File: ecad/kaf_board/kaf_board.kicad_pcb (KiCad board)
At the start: 4 copper layers, 116 x 71 mm, 234 parts, among them J1 PWR, J2 TEC1, J3 Conn_01x12, J4 TEC2, J5 USB, J6 TECPWR, M1 Motor_Servo, M2 Servo cut-out, Q1 MMBT3904LT1G, Q2 NTD4804N, Q3 NTD4804N, U1 MAX4649, U10 LM224, U11 LM224, U12 LM224, U13 LD1117S12CTR_SOT223, U14 LD1117S33CTR_SOT223, U15 LTC3265*FE, U16 93LCxxBxxOT, U17 FT2232HL, U18 ICE40HX1K-VQ100, U19 W25X20CL, U2 ADP7118AUJZ, U20 MCP3004, U21 TC4427, U3 AD9826, U4 KAF-CDIP24, U5 TL432LIAIDBZR, U6 TL432LIAIDBZR, U7 TC4427, U8 TC4427, U9 TC4428, X1 KC7050A-C3, Y1 12 MHz

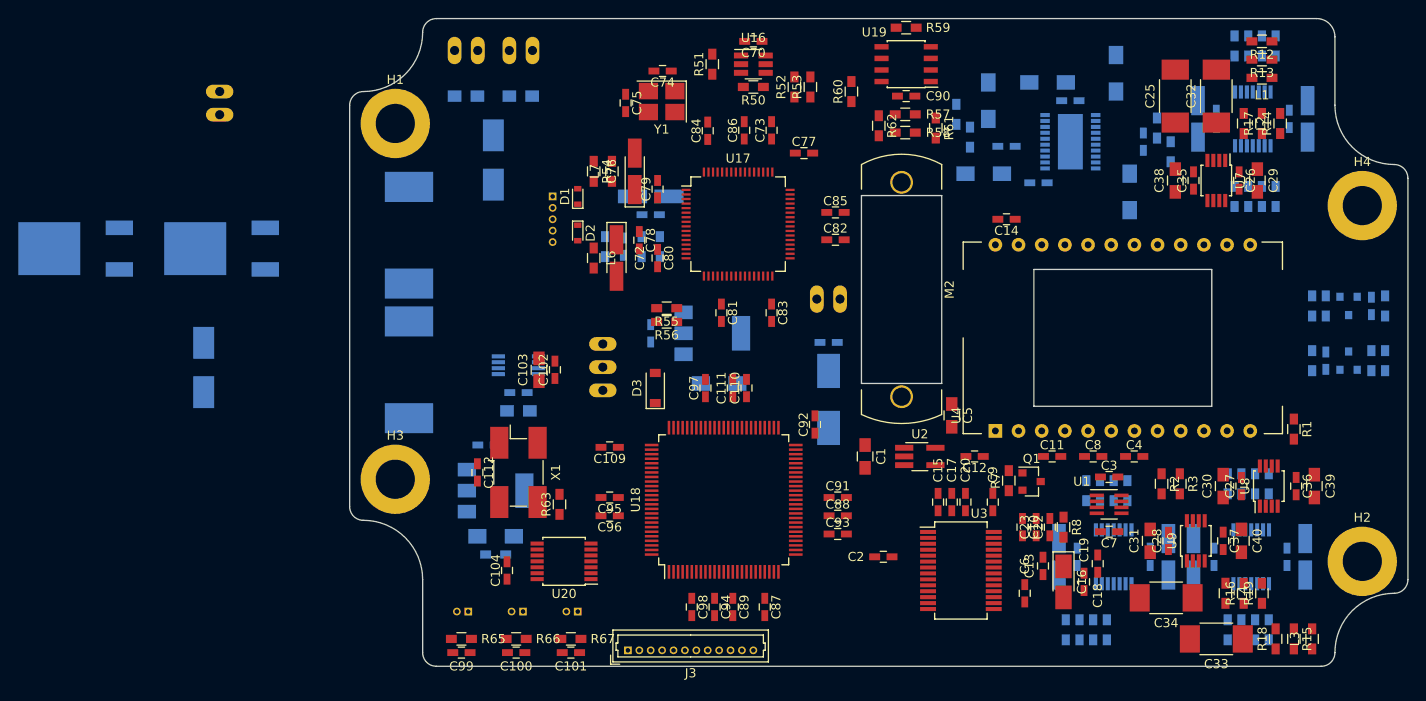
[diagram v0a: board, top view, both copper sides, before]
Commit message: Started routing PCB
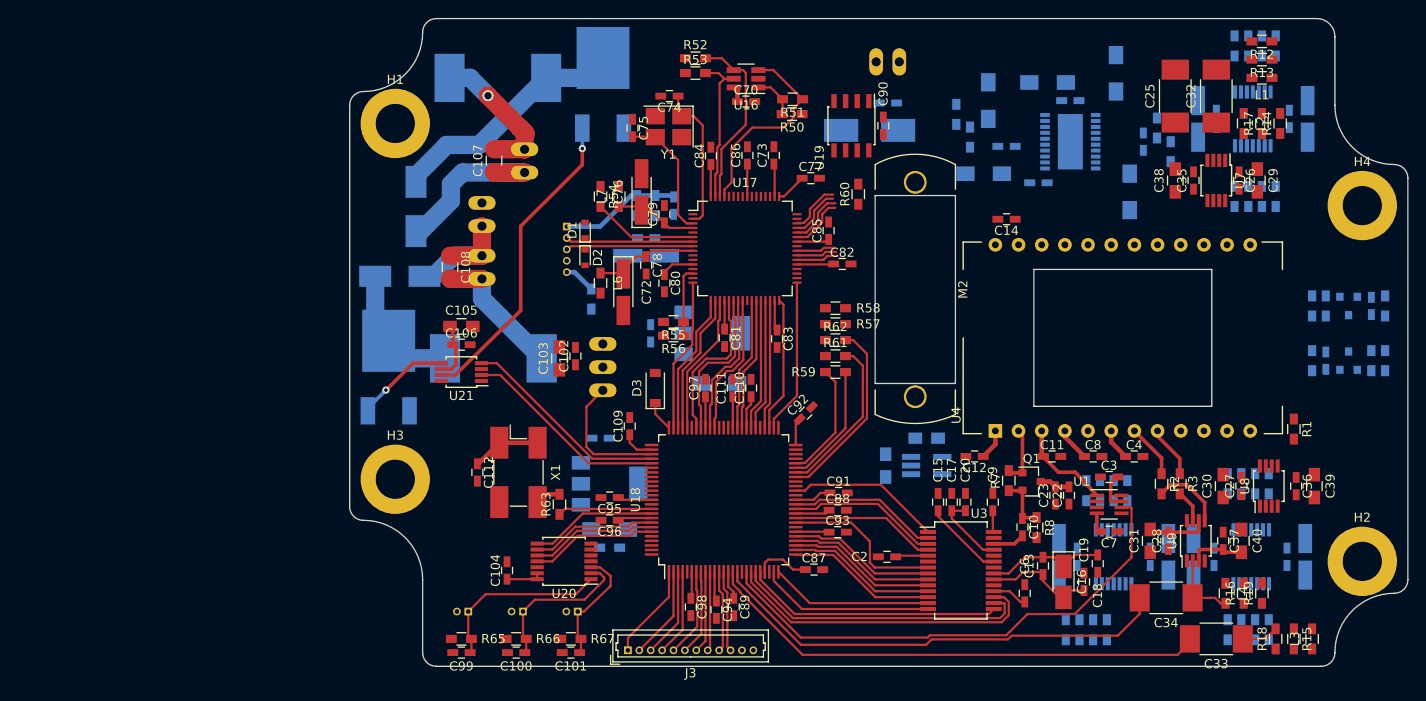
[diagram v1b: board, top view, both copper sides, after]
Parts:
- C1, C5, U2: moved to B.Cu
- C105, C106, C107, C108, U21: moved to F.Cu
- moved Q2 53.1 mm to (117.5, 79.0), turned to 270 degrees
- moved R59 38.5 mm to (145.2, 105.8), turned to 0 degrees
- moved J6 32.3 mm to (106.5, 89.8), turned to 90 degrees
- moved C69 29.8 mm to (149.0, 79.2), turned to 180 degrees
- moved R61 27.3 mm to (145.2, 104.0), turned to 0 degrees
- moved C68 27.0 mm to (151.0, 76.2)
- moved J1 26.8 mm to (152.2, 71.8)
- moved R57 24.2 mm to (145.2, 100.5)
- moved R62 24.0 mm to (145.2, 102.2), turned to 0 degrees
- moved D5 23.7 mm to (97.5, 95.2), turned to 180 degrees
- moved J4 22.7 mm to (106.5, 93.0), turned to 270 degrees
- moved R58 20.7 mm to (145.2, 98.8)
- moved C108 20.3 mm to (103.0, 94.2), turned to 270 degrees
- moved L8 19.8 mm to (108.2, 73.5), turned to 90 degrees
- moved Q3 19.2 mm to (94.0, 110.0), turned to 270 degrees
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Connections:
- Q2 pad 2: (no net) -> Net-(D4-Pad2)
- Q3 pad 2: (no net) -> Net-(D5-Pad2)
- R55 pad 2: (no net) -> /usb-interface/VUSB
- U18 pad 100: /fpga/PWM_SERVO -> (no net)
- U18 pad 15: /ccd/AMP_OFF -> /ccd/R_3.3V
- U18 pad 18: /ccd/R_3.3V -> /ccd/AMP_OFF
- U18 pad 78: (no net) -> /fpga/PWM_SERVO
- U18 pad 79: (no net) -> /fpga/PWM_TEC2
- U18 pad 80: (no net) -> /fpga/PWM_TEC1
- U18 pad 97: /fpga/PWM_TEC1 -> (no net)
- U18 pad 99: /fpga/PWM_TEC2 -> (no net)
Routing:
- net +3V3: track 0.00 -> 71.7 mm
- net /ccd/AMP_OFF: track 0.00 -> 56.1 mm
- net /ccd/R_3.3V: track 0.00 -> 55.7 mm
- net /ccd/H_3.3V: track 0.00 -> 51.2 mm
- net /thermo_and_mechanical/V_TEC: track 0.00 -> 39.2 mm
- net /ccd/AD_SLOAD: track 0.00 -> 34.8 mm
- net Net-(Q2-Pad1): track 0.00 -> 34.4 mm, vias 0 -> 1
- net /ccd/AD_SCLK: track 0.00 -> 32.5 mm
- net Net-(D4-Pad2): track 0.00 -> 28.5 mm
- net /ccd/AD_SDATA: track 0.00 -> 28.2 mm
- net /usb-interface/FT_CDONE: track 0.00 -> 26.3 mm
- net /usb-interface/FT_CRESET: track 0.00 -> 23.6 mm
- net /fpga/PWM_TEC2: track 0.00 -> 23.0 mm
- net /fpga/PWM_TEC1: track 0.00 -> 22.7 mm
- net Net-(R51-Pad1): track 0.00 -> 22.4 mm
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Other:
- outline, holes or cut-outs redrawn

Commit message: continued routing
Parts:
- moved R60 24.4 mm to (146.6, 110.6)
- moved C90 22.1 mm to (142.6, 99.4), turned to 270 degrees
- moved U19 20.6 mm to (146.1, 99.3), turned to 90 degrees
- moved R61 12.0 mm to (151.8, 114.0), turned to 180 degrees
- moved R62 11.2 mm to (150.3, 112.3), turned to 180 degrees
- moved R59 9.09 mm to (146.1, 114.8)
- moved R58 8.19 mm to (143.5, 106.8)
- moved R57 7.90 mm to (143.5, 108.2)
- moved R19 4.00 mm to (188.0, 130.0), turned to 270 degrees
- moved L3 2.25 mm to (195.2, 135.0)
- moved L4 1.75 mm to (189.8, 130.0)
- moved C82 1.53 mm to (144.5, 94.2)
- moved R15 1.50 mm to (197.0, 135.0)
- moved R16 1.50 mm to (191.5, 130.0)
- moved C85 1.35 mm to (145.0, 91.5), turned to 0 degrees
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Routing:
- net /fpga/V1_3.3V: track 0.00 -> 77.0 mm
- net /ccd/V1_3.3V: track 0.00 -> 74.9 mm
- net /usb-interface/FT_SCK: track 4.65 -> 36.2 mm
- net Net-(R1-Pad1): track 0.00 -> 24.0 mm
- net /usb-interface/FT_SS: track 6.07 -> 27.8 mm, vias 0 -> 2
- net /usb-interface/FT_CRESET: track 23.6 -> 42.8 mm
- net /usb-interface/FT_MOSI: track 17.9 -> 36.2 mm
- net Net-(C33-Pad1): track 4.06 -> 19.8 mm
- net /usb-interface/FT_CDONE: track 26.3 -> 41.8 mm, vias 0 -> 2
- net /usb-interface/FT_MISO: track 17.1 -> 30.6 mm, vias 0 -> 2
- net Net-(R60-Pad2): track 0.00 -> 13.5 mm
- net /ccd/V_RH: track 0.00 -> 6.79 mm
- net Net-(R57-Pad1): track 0.00 -> 6.37 mm
- net (no net): track 6.07 -> 0.00 mm
- net Net-(C25-Pad1): track 0.00 -> 5.61 mm
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
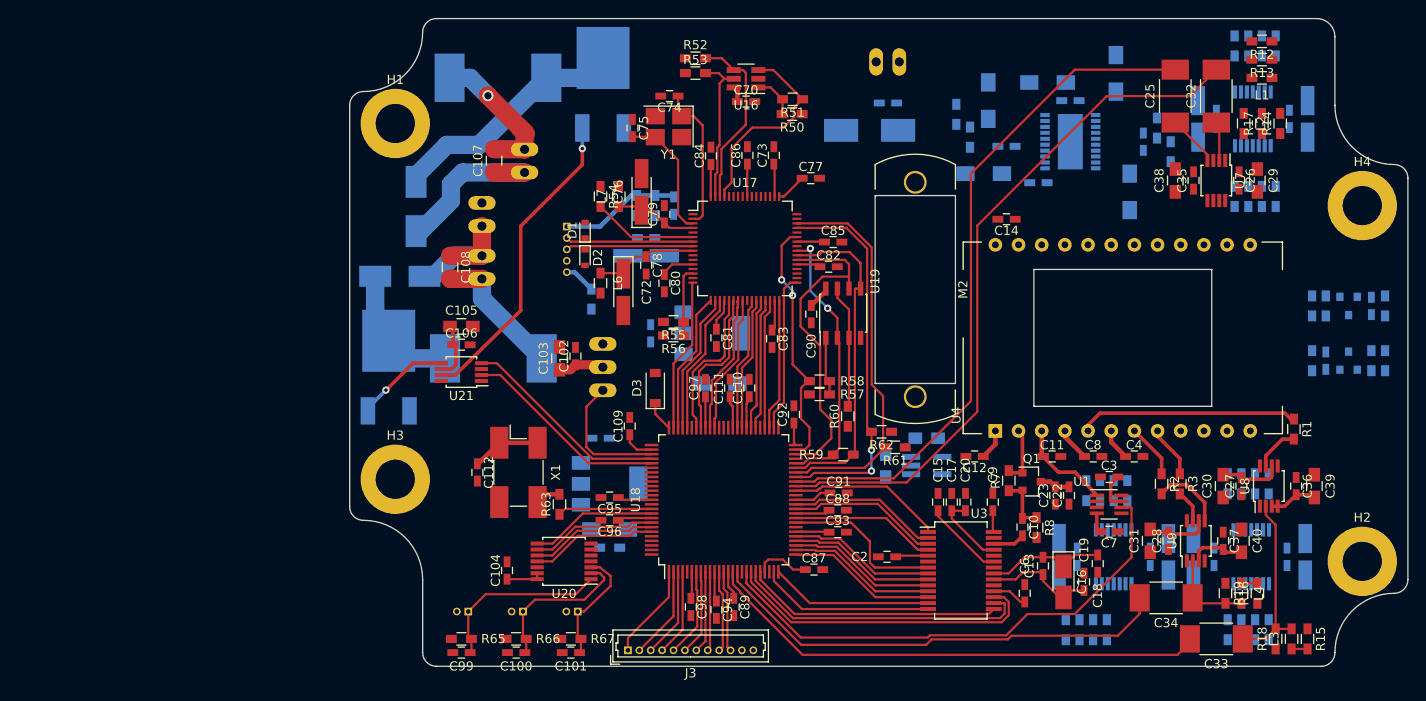
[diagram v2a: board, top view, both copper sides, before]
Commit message: Changed +-15 DC/DC converter and routed it.
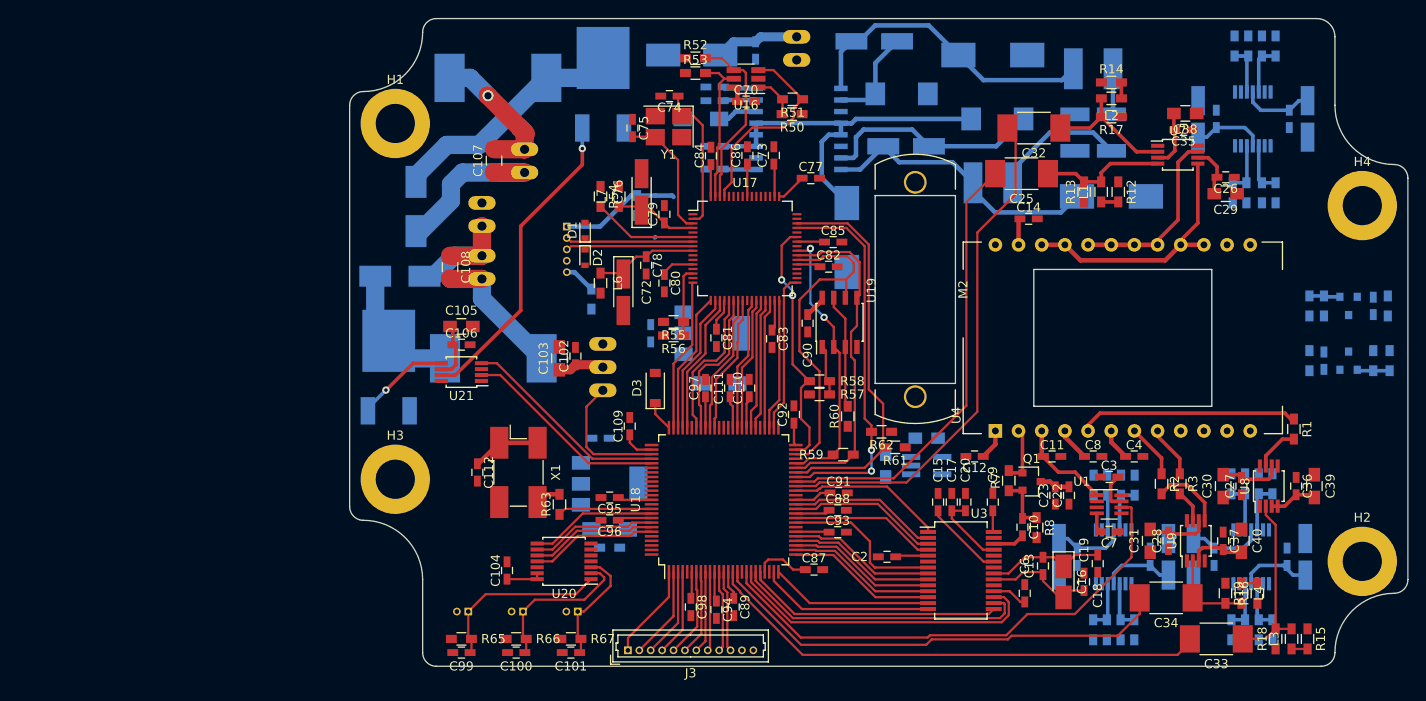
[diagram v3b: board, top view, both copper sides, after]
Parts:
- removed C67: 4.7u, Capacitors_Tantalum_SMD:CP_Tantalum_Case-A_EIA-3216-18_Hand
- removed C71: 10n, Capacitors_SMD:C_0603_HandSoldering
- removed R45, R48: 604k, Resistors_SMD:R_0603_HandSoldering
- removed R46, R47: 52.3k, Resistors_SMD:R_0603_HandSoldering
- added D6: SS14, Diodes_SMD:D_SMA_Handsoldering, B.Cu at (153.0, 81.0)
- added D7: SS14, Diodes_SMD:D_SMA_Handsoldering, B.Cu at (149.5, 69.5)
- added L10: 100u, kaf_board:L_Bourns_SRR0604, B.Cu at (152.5, 75.2)
- added L11: 33u, kaf_board:L_Wuerth_LQS_5040, B.Cu at (162.5, 85.0)
- added L12: 33u, kaf_board:L_Wuerth_LQS_5040, B.Cu at (173.5, 72.5)
- C53: value 10u -> 10n; footprint Capacitors_SMD:C_1206_HandSoldering -> Capacitors_SMD:C_0603_HandSoldering
- C54: value 10u -> 0.1u; footprint Capacitors_SMD:C_1206_HandSoldering -> Capacitors_SMD:C_0603_HandSoldering
- C55: value 1u -> 10u; footprint Capacitors_SMD:C_0603_HandSoldering -> Capacitors_SMD:C_1206_HandSoldering
- C56: value 10u -> 1u; footprint Capacitors_SMD:C_1206_HandSoldering -> Capacitors_SMD:C_0603_HandSoldering
- C59: value 1u -> 10n
- C62, C63: value 10u -> 100u; footprint Capacitors_SMD:C_1206_HandSoldering -> Capacitors_Tantalum_SMD:CP_Tantalum_Case-D_EIA-7343-31_Hand
- C64: value 0.1u -> 100u; footprint Capacitors_SMD:C_0603_HandSoldering -> Capacitors_Tantalum_SMD:CP_Tantalum_Case-D_EIA-7343-31_Hand
- C65, C66: value 0.1u -> 2.2u; footprint Capacitors_SMD:C_0603_HandSoldering -> Capacitors_Tantalum_SMD:CP_Tantalum_Case-A_EIA-3216-18_Hand
- L5: value 1K/0.8A -> 100u; footprint Inductors_SMD:L_0603_HandSoldering -> kaf_board:L_Bourns_SRR0604
- U15: value LTC3265*FE -> MAX743; footprint kaf_board:TSSOP-20-1EP_4.4x6.5mm_P0.65mm -> Housings_SOIC:SOIC-16W_7.5x10.3mm_Pitch1.27mm
- moved C66 50.8 mm to (173.5, 77.5), turned to 0 degrees
- moved C54 44.7 mm to (132.0, 81.0), turned to 180 degrees
- moved C55 40.5 mm to (130.5, 78.0)
- moved L5 38.7 mm to (163.0, 78.0)
- moved C59 37.0 mm to (132.0, 74.5), turned to 180 degrees
- moved C56 36.6 mm to (132.0, 76.0), turned to 180 degrees
- moved U15 29.8 mm to (141.2, 79.1), turned to 0 degrees
- moved C53 29.5 mm to (132.0, 83.5)
- moved R13 24.3 mm to (172.5, 86.0), turned to 90 degrees
- moved R12 22.8 mm to (176.2, 86.0), turned to 270 degrees
- moved L1 21.6 mm to (174.4, 86.0), turned to 90 degrees
- moved C62 21.6 mm to (146.5, 91.0), turned to 270 degrees
- moved C63 21.2 mm to (162.5, 71.0), turned to 180 degrees
- moved C69 21.2 mm to (129.5, 71.0)
- moved C32 20.3 mm to (167.0, 79.0), turned to 180 degrees
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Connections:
- net Net-(C76-Pad1) renamed /usb-interface/VPHY
- net Net-(D3-Pad1) renamed /fpga/VPP_2V5
- C1 pad 2: +12V -> +6V
- C102 pad 1: +5V -> +6V
- C103 pad 1: +5V -> +6V
- C53 pad 1: +12V -> Net-(C53-Pad1)
- C54 pad 1: Net-(C54-Pad1) -> +6V
- C55 pad 2: Net-(C55-Pad2) -> GND
- C57 pad 1: +5V -> +6V
- C58 pad 1: +5V -> +6V
- C59 pad 2: Net-(C59-Pad2) -> GND
- C62 pad 1: -15V -> +6V
- C63 pad 1: +15V -> GND
- C63 pad 2: GND -> Net-(C63-Pad2)
- C65 pad 1: GND -> +15V
- C65 pad 2: Net-(C65-Pad2) -> GND
- C66 pad 1: +5V -> GND
- C66 pad 2: GND -> -15V
- C68 pad 1: +12V -> +6V
- C69 pad 1: +12V -> +6V
- J1 pad 1: +12V -> +6V
- L5 pad 1: /usb-interface/VUSB -> +6V
- L5 pad 2: +5V -> Net-(D6-Pad2)
- M1 pad 2: +5V -> +6V
- U13 pad 3: +5V -> +6V
- U14 pad 3: +5V -> +6V
- U15 pad 1: Net-(C59-Pad2) -> Net-(C53-Pad1)
- U15 pad 10: Net-(C55-Pad2) -> Net-(D7-Pad1)
- U15 pad 11: Net-(C55-Pad1) -> GND
- U15 pad 12: Net-(C55-Pad1) -> +6V
- U15 pad 13: Net-(C54-Pad1) -> +6V
- U15 pad 15: +12V -> Net-(D6-Pad2)
- U15 pad 16: GND -> Net-(C64-Pad1)
- U15 pad 2: Net-(C59-Pad2) -> GND
- U15 pad 3: Net-(C59-Pad1) -> +6V
- U15 pad 4: +12V -> +6V
- U15 pad 5: +12V -> +6V
- U15 pad 6: Net-(C65-Pad2) -> Net-(C55-Pad1)
- U15 pad 7: Net-(R47-Pad2) -> Net-(C56-Pad1)
- U15 pad 8: -15V -> Net-(C59-Pad1)
- U15 pad 9: Net-(C56-Pad1) -> Net-(C63-Pad2)
- U2 pad 1: +12V -> +6V
- U2 pad 3: +12V -> +6V
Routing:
- net +6V: track 0.00 -> 55.8 mm
- net +15V: track 5.52 -> 44.4 mm
- net Net-(C63-Pad2): track 0.00 -> 33.7 mm
- net Net-(C64-Pad1): track 0.00 -> 31.1 mm
- net -15V: track 4.10 -> 33.3 mm
- net /ccd/V1: track 0.00 -> 28.9 mm
- net /ccd/V1_3.3V: track 74.9 -> 48.9 mm
- net Net-(D6-Pad2): track 0.00 -> 24.5 mm
- net /fpga/V1_3.3V: track 77.0 -> 56.5 mm
- net /ccd/V2: track 0.00 -> 20.2 mm
- net Net-(D7-Pad1): track 0.00 -> 10.8 mm
- net Net-(C32-Pad1): track 4.28 -> 14.8 mm
- net Net-(C25-Pad1): track 5.61 -> 14.4 mm
- net /ccd/V_VL: track 0.00 -> 6.33 mm
- net Net-(R32-Pad2): track 0.00 -> 5.69 mm
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
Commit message: Power plane design and started routing the CCD circuit supplies
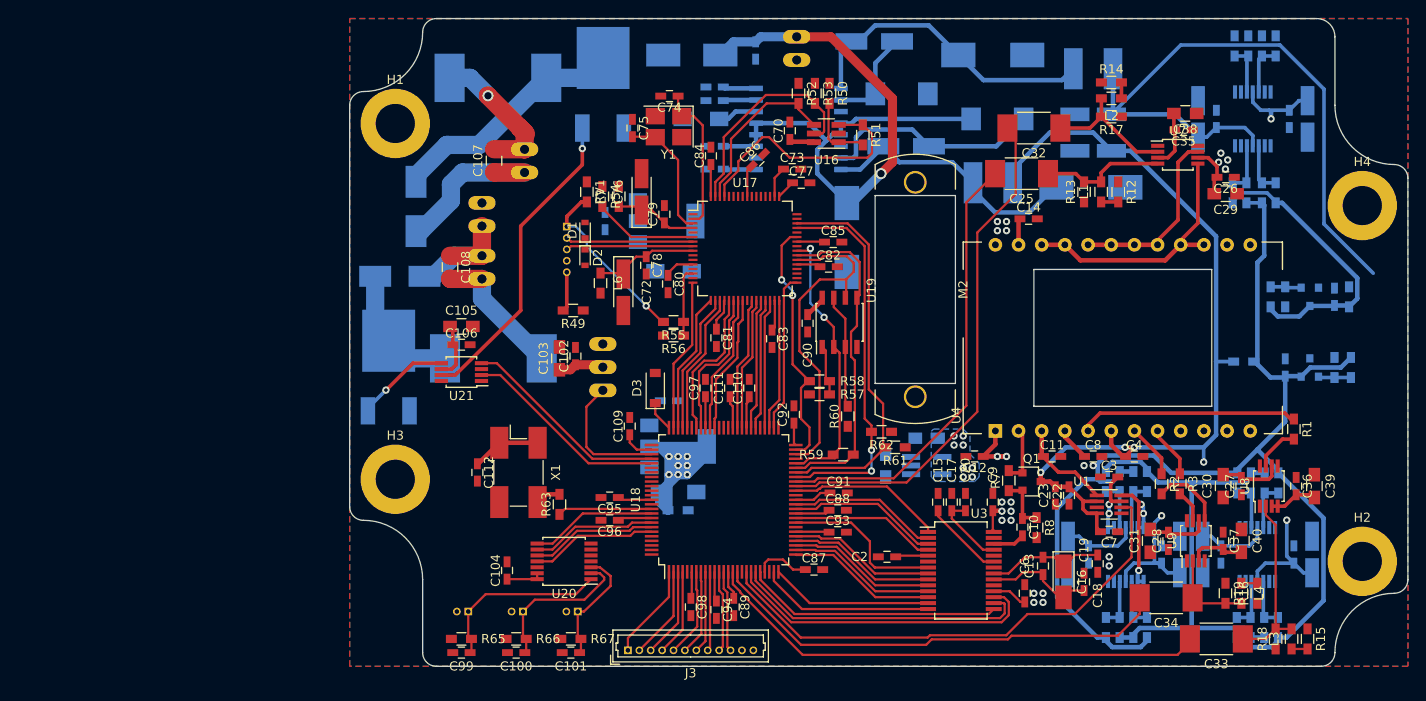
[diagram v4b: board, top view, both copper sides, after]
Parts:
- R49, RV1: moved to F.Cu
- moved C49 15.8 mm to (195.5, 125.8)
- moved C50 15.8 mm to (187.5, 125.8)
- moved C51 15.8 mm to (197.5, 125.8)
- moved C52 15.8 mm to (185.5, 125.8)
- moved R36 15.8 mm to (193.8, 133.8)
- moved R37 15.8 mm to (192.2, 133.8)
- moved R38 15.8 mm to (189.2, 133.8)
- moved R39 15.8 mm to (190.8, 133.8)
- moved R40 15.8 mm to (189.3, 117.9)
- moved R41 15.8 mm to (190.8, 117.9)
- moved R42 15.8 mm to (193.8, 117.9)
- moved R43 15.8 mm to (192.3, 117.9)
- moved U12 15.8 mm to (191.5, 125.8)
- moved C41 13.8 mm to (181.0, 125.8)
- moved C42 13.8 mm to (173.0, 125.8)
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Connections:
- net /ccd/ccd_voltage_1/V2 renamed /ccd/VOG
- net /ccd/ccd_voltage_1/V3 renamed /ccd/VRD
- net /ccd/ccd_voltage_1/V4 renamed /ccd/VSS
- net Net-(C5-Pad2) renamed /ccd/AVDD
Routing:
- net /ccd/+V_REF: track 0.00 -> 127.8 mm
- net +15V: track 44.4 -> 162.4 mm, vias 0 -> 5
- net /ccd/-V_REF: track 0.00 -> 84.5 mm
- net -15V: track 33.3 -> 94.7 mm
- net +1V2: track 14.2 -> 53.5 mm, vias 0 -> 8
- net +6V: track 55.8 -> 82.3 mm, vias 0 -> 1
- net /ccd/V_AMPL: track 0.00 -> 11.6 mm, vias 0 -> 1
- net Net-(R53-Pad2): track 16.7 -> 23.9 mm
- net /usb-interface/VUSB: track 13.2 -> 19.5 mm, vias 0 -> 1
- net /ccd/VSS: track 3.45 -> 9.55 mm, vias 0 -> 4
- net Net-(R51-Pad1): track 22.4 -> 27.5 mm
- net /ccd/VRD: track 3.69 -> 6.94 mm, vias 0 -> 4
- net Net-(R50-Pad2): track 4.83 -> 7.96 mm
- net /ccd/VOG: track 3.35 -> 6.40 mm, vias 0 -> 4
- net GND: track 0.00 -> 2.97 mm
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- added copper zone on In2.Cu, net +1V2
- added copper zone on In2.Cu, net +3V3
- added copper zone on In2.Cu, net +6V
- added copper zone on B.Cu, net /ccd/AVDD
- added copper zone on In2.Cu, net /ccd/AVDD
- added copper zone on In2.Cu, net /ccd/VGUARD
- added copper zone on In2.Cu, net /ccd/VOG
- added copper zone on In2.Cu, net /ccd/VRD
- added copper zone on In2.Cu, net /ccd/VSS
- added copper zone on In2.Cu, net /thermo_and_mechanical/V_TEC
- added copper zone on B.Cu, net GND
- added copper zone on F.Cu, net GND
- added copper zone on In1.Cu, net GND
- added copper zone on In2.Cu, net GND
